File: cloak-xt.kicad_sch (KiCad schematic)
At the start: 21 parts, among them J1 USB_C_Receptacle_USB2.0, U1 STM32F072CBT6, U2 PRTR5V0U2X

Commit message: Init matrix
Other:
- added sheet switches (switches.kicad_sch)
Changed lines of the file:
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@@
+    )
+  )
+  (sheet (at 194.945 46.355) (size 49.53 38.1) (fields_autoplaced)
+    (stroke (width 0.1524) (type solid))
+    (fill (color 0 0 0 0.0000))
+    (property "Sheetname" "switches" (at 194.945 45.6434 0)
+      (effects (font (size 1.27 1.27)) (justify left bottom))
+    )
+    (property "Sheetfile" "switches.kicad_sch" (at 194.945 85.0396 0)
+      (effects (font (size 1.27 1.27)) (justify left top))
+    )
+    (instances
+      (project "cloak-xt"
+        (path "/4d291fcf-fdf2-46ba-aa57-60bc75f9cc32" (page "2"))
+      )
     )
   )

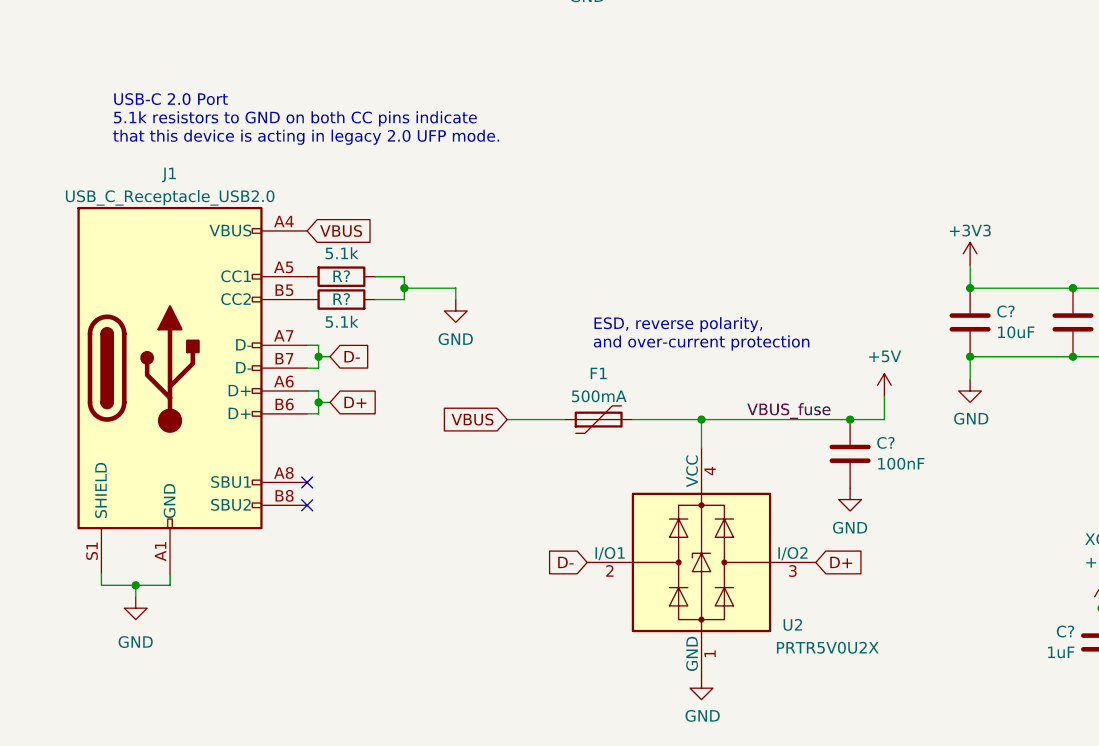
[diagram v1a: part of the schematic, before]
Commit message: Remove onboard USB/ESD and add JST
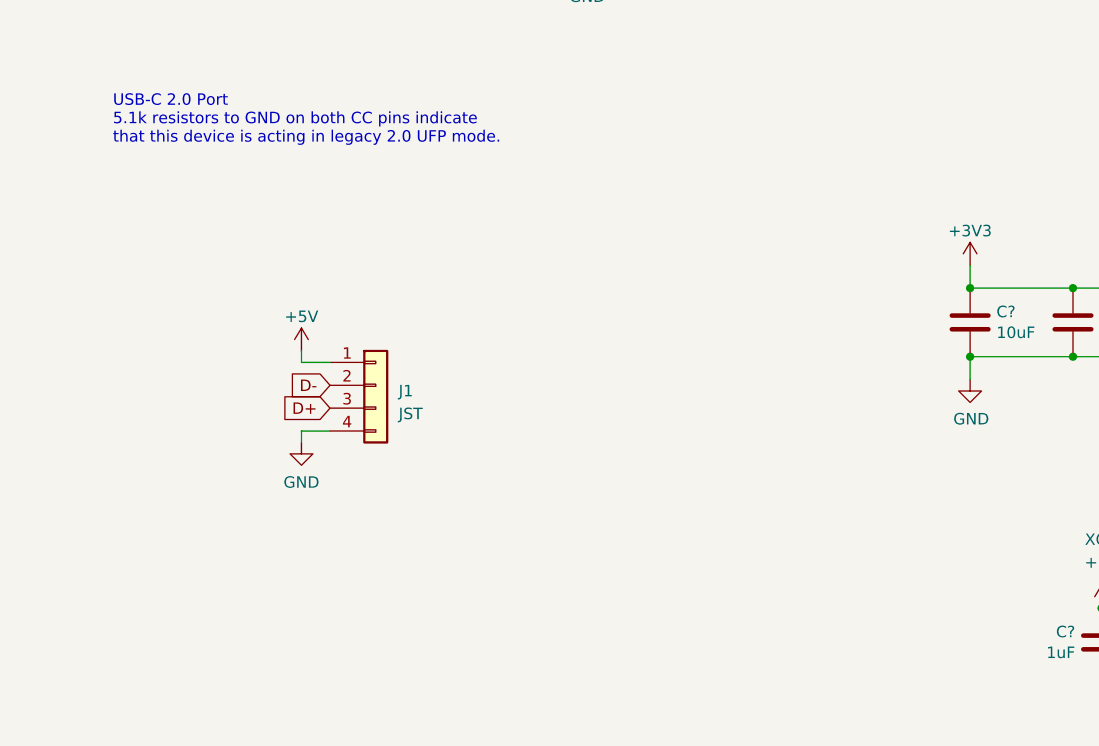
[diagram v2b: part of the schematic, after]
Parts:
- removed C?: 100nF, Capacitor_SMD:C_0402_1005Metric, symbol Device:C
- removed F1: 500mA, Fuse:Fuse_1206_3216Metric, symbol Device:Polyfuse
- removed J1: USB_C_Receptacle_USB2.0, Connector_USB:USB_C_Receptacle_HRO_TYPE-C-31-M-12, symbol Connector:USB_C_Receptacle_USB2.0
- removed R? (x2): 5.1k, Resistor_SMD:R_0402_1005Metric, symbol Device:R
- removed U2: PRTR5V0U2X, Package_TO_SOT_SMD:SOT-143, symbol Power_Protection:PRTR5V0U2X
- added J1: JST, symbol Connector_Generic:Conn_01x04
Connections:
- net +5V: now also J1.1 (Pin_1)
- net D+: now also J1.3 (Pin_3)
- net D-: now also J1.2 (Pin_2)
- net GND: now also J1.4 (Pin_4)
- no-connect marks 2 -> 0
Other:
- note removed: "ESD, reverse polarity, and over-current protection"

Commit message: Update JST on PCB
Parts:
- J1: footprint (none) -> Connector_JST:JST_SH_SM04B-SRSS-TB_1x04-1MP_P1.00mm_Horizontal
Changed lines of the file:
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@@
       (effects (font (size 1.27 1.27)) (justify left))
     )
-    (property "Footprint" "" (at 55.88 153.67 0)
+    (property "Footprint" "Connector_JST:JST_SH_SM04B-SRSS-TB_1x04-1MP_P1.00mm_Horizontal" (at 55.88 153.67 0)
       (effects (font (size 1.27 1.27)) hide)
     )

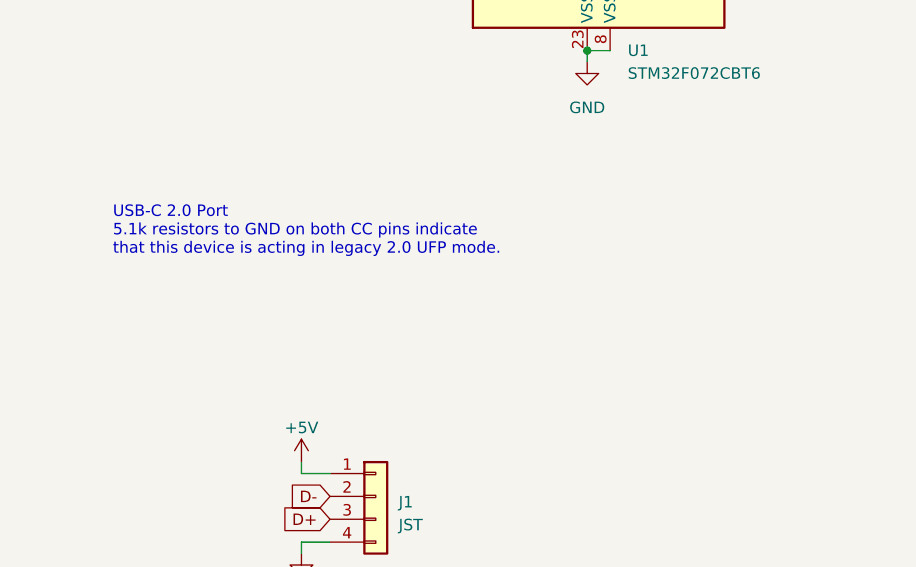
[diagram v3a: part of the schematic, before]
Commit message: Complete matrix and add Skyloong knob module
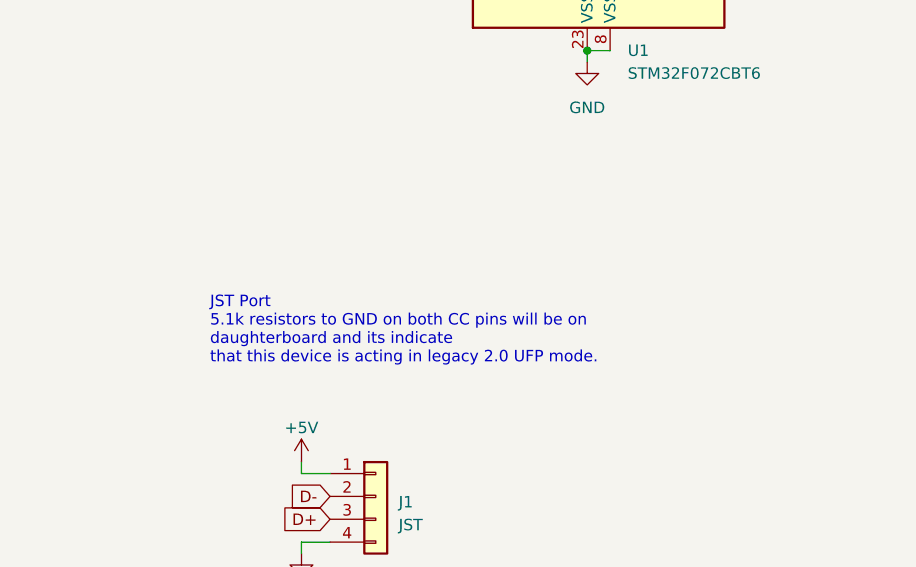
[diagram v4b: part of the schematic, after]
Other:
- note added: "JST Port 5.1k resistors to GND on both CC pins will be on daughterboard and its indicate that this device is acting in legacy 2.0 UFP mode."
- note removed: "USB-C 2.0 Port 5.1k resistors to GND on both CC pins indicate that this device is acting in legacy 2.0 UFP mode."
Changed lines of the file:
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@@
     (effects (font (size 1.27 1.27)) (justify left bottom))
   )
-  (text "USB-C 2.0 Port\n5.1k resistors to GND on both CC pins indicate\nthat this device is acting in legacy 2.0 UFP mode."
-    (at 26.67 127 0)
+  (text "JST Port\n5.1k resistors to GND on both CC pins will be on\ndaughterboard and its indicate\nthat this device is acting in legacy 2.0 UFP mode."
+    (at 37.465 139.065 0)
     (effects (font (size 1.27 1.27)) (justify left bottom))
   )

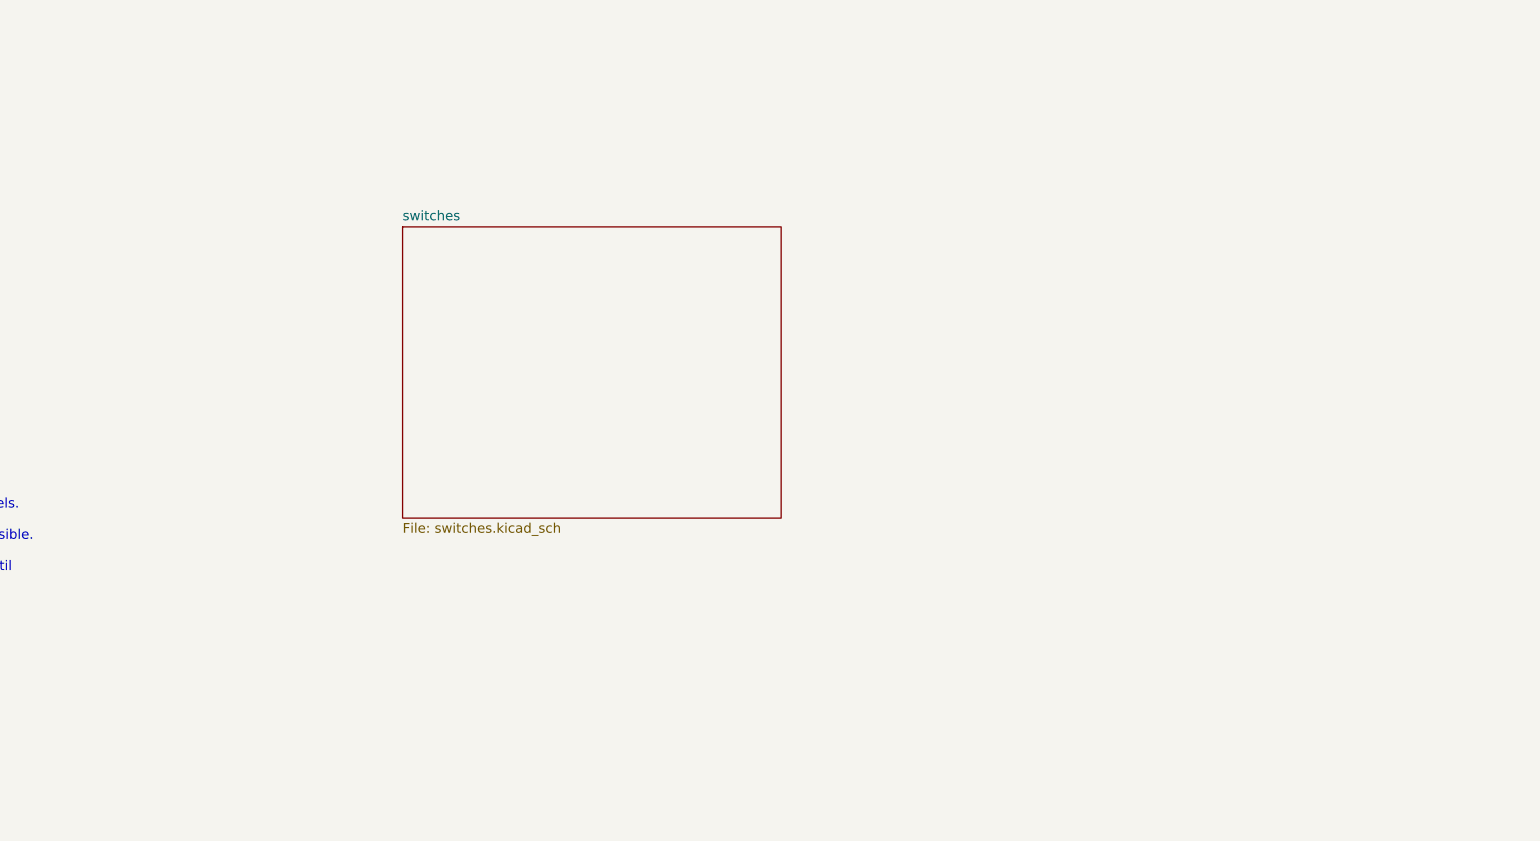
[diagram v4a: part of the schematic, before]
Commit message: Change switches text placement
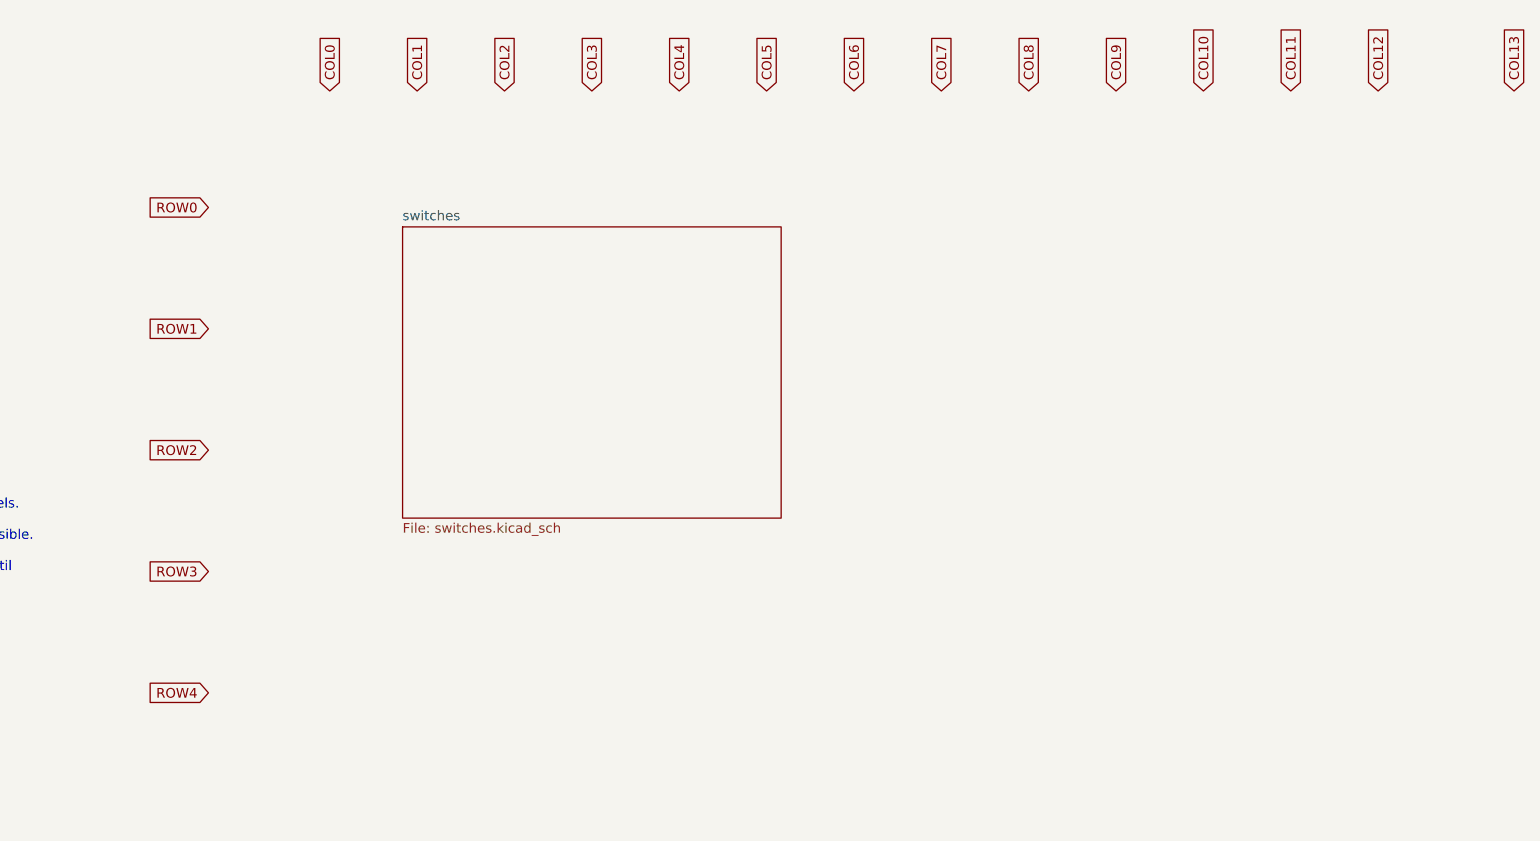
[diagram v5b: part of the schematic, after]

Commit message: Complete BOOT/RST traces
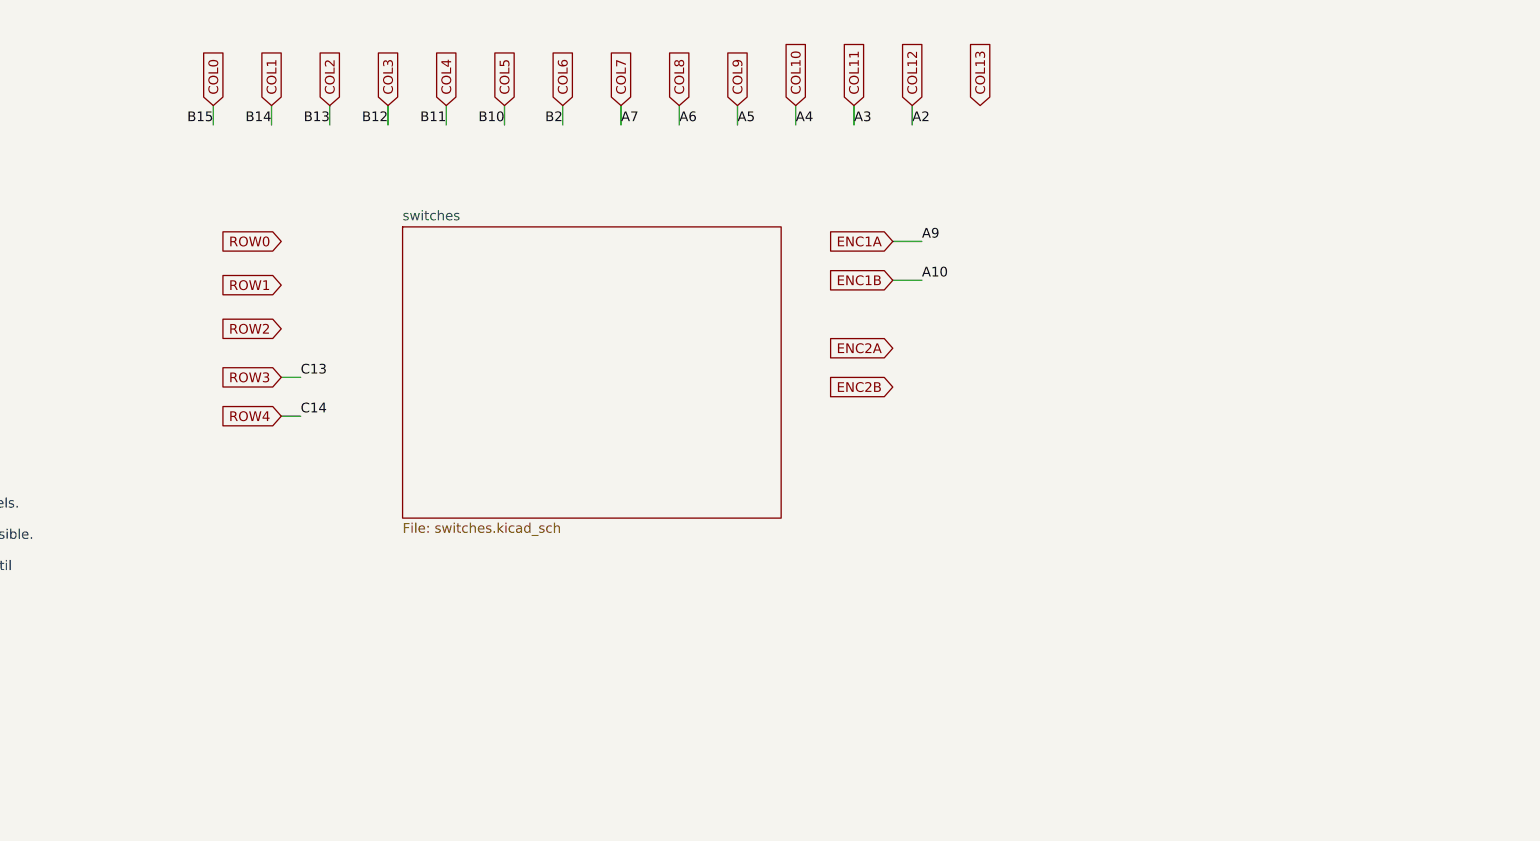
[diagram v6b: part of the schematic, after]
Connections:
- net A2 is gone; now on net COL12: U1.12 (PA2)
- net A3 is gone; now on net COL11: U1.13 (PA3)
- net A4 is gone; now on net COL10: U1.14 (PA4)
- net A5 is gone; now on net COL9: U1.15 (PA5)
- net A6 is gone; now on net COL8: U1.16 (PA6)
- net A7 is gone; now on net COL7: U1.17 (PA7)
- net B10 is gone; now on net COL5: U1.21 (PB10)
- net B11 is gone; now on net COL4: U1.22 (PB11)
- net B12 is gone; now on net COL3: U1.25 (PB12)
- net B13 is gone; now on net COL2: U1.26 (PB13)
- net B14 is gone; now on net COL1: U1.27 (PB14)
- net B15 is gone; now on net COL0: U1.28 (PB15)
- net B2 is gone; now on net COL6: U1.20 (PB2)
- net C13 is gone; now on net ROW3: U1.2 (PC13)
- net C14 is gone; now on net ROW4: U1.3 (PC14)
- net A10 renamed ENC1B
- net A9 renamed ENC1A
